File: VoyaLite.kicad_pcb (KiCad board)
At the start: 4 copper layers, 141.4 x 143 mm, 72 parts, among them J1 Conn_01x02_Socket, J3 USB_C_Receptacle_USB2.0_16P, J4 Conn_01x04_Socket, Q1 NTJD1155LT1G, Q2 NTJD1155LT1G, SW1 SW_SPDT_312, SW2 SW_SPDT_312, U1 WE-TVS-82400102, U2 E73-2G4M08S1C, U3 BQ24075RGT, U4 XC6220B331MR, Y1 32.768kHz

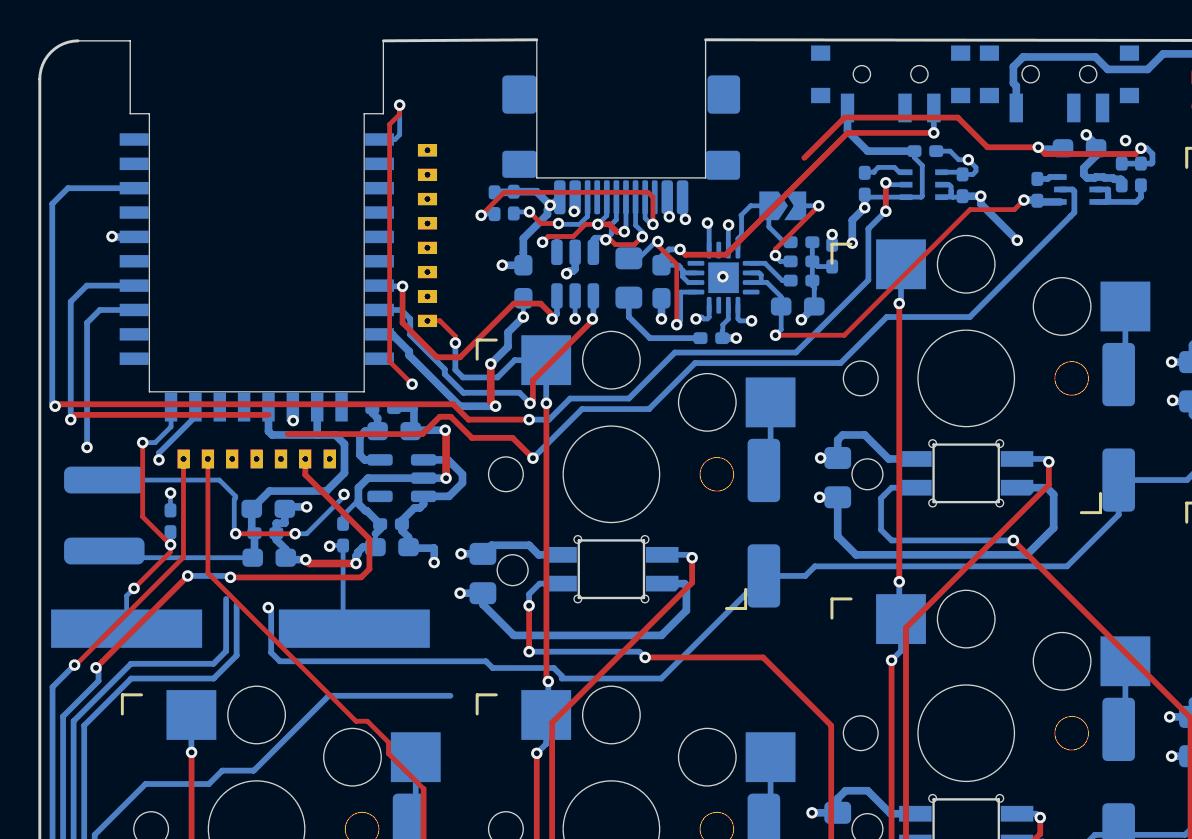
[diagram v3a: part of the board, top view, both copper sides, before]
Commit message: add voyalite
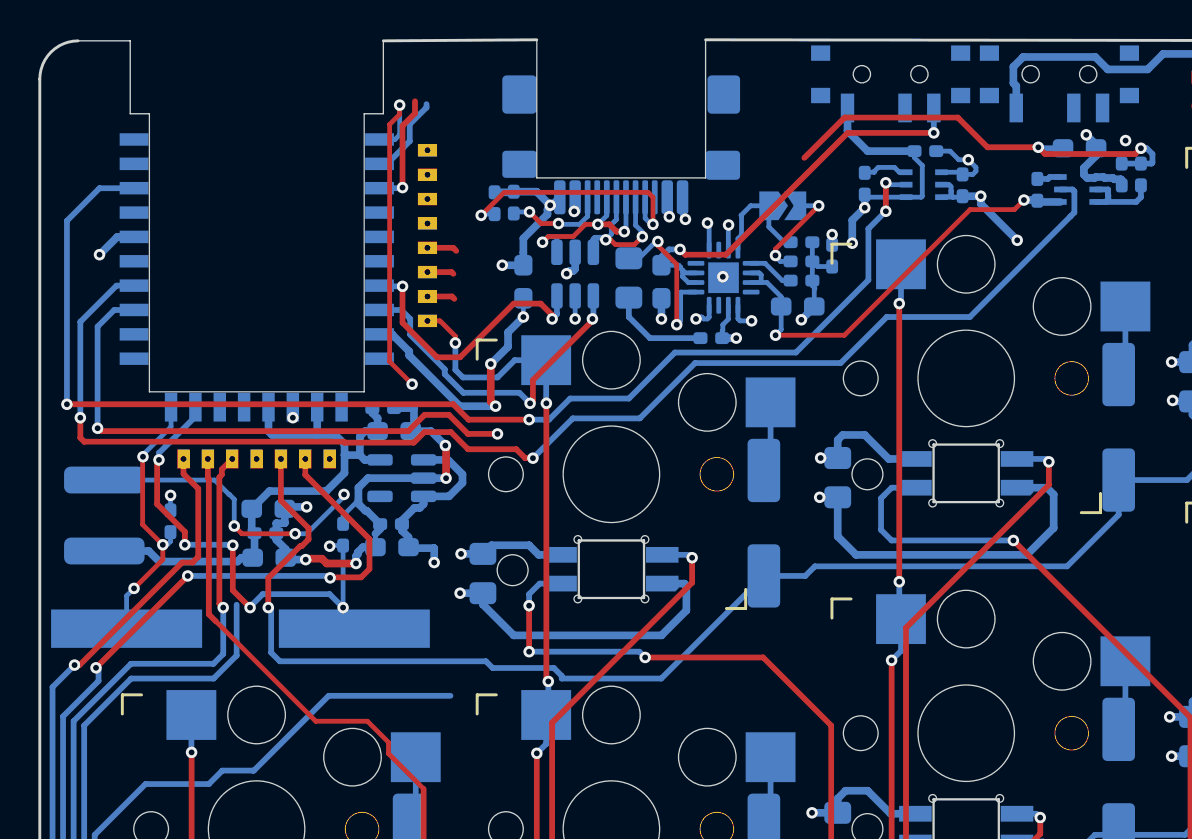
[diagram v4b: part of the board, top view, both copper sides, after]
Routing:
- net BAT_MEAS_ADC: track 32.7 -> 52.7 mm, vias 3 -> 4
- net Net-(U2B-P0.01/XL2): track 8.83 -> 25.6 mm, vias 2 -> 6
- net r5: track 127.3 -> 136.5 mm
- net r2: track 274.9 -> 282.5 mm, vias 0 -> 1
- net Net-(J4-Pin_4): track 13.3 -> 19.3 mm, vias 0 -> 1
- net r3: track 182.4 -> 186.7 mm
- net LED_EN: track 67.6 -> 65.5 mm
- net c5: track 75.3 -> 76.9 mm
- net GND: track 1316.1 -> 1317.5 mm
- net c3: track 75.2 -> 76.6 mm
- net c4: track 75.5 -> 76.9 mm
- net BAT_MEAS_EN: track 70.8 -> 69.5 mm
- net LED: track 88.9 -> 90.1 mm
- net c7: track 226.4 -> 227.6 mm
- net +3V3: track 29.1 -> 30.0 mm

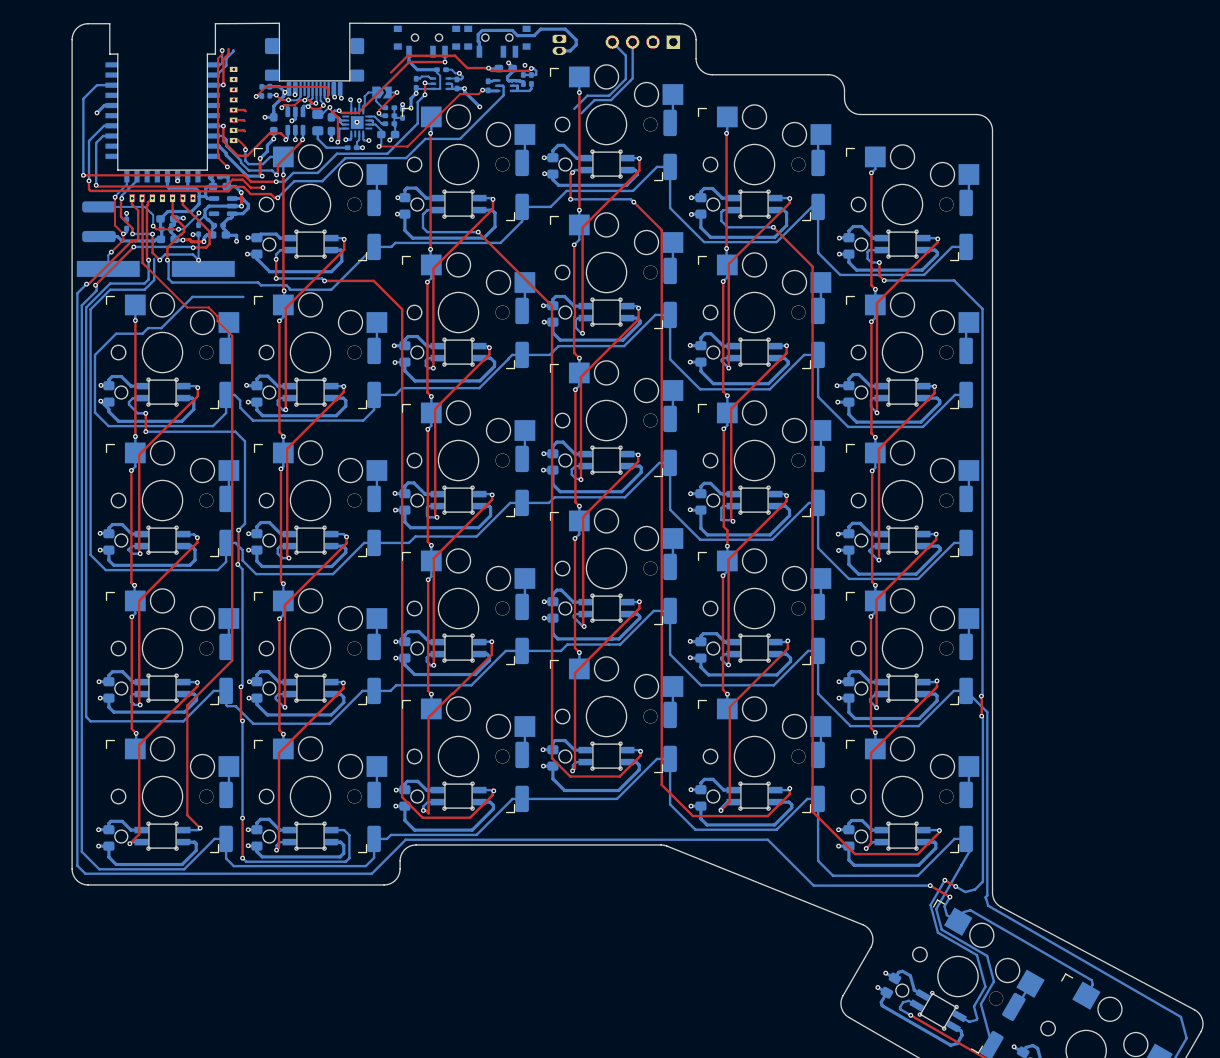
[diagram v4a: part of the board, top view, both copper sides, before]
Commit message: add changes to voyalite. Add nrf52840 plus
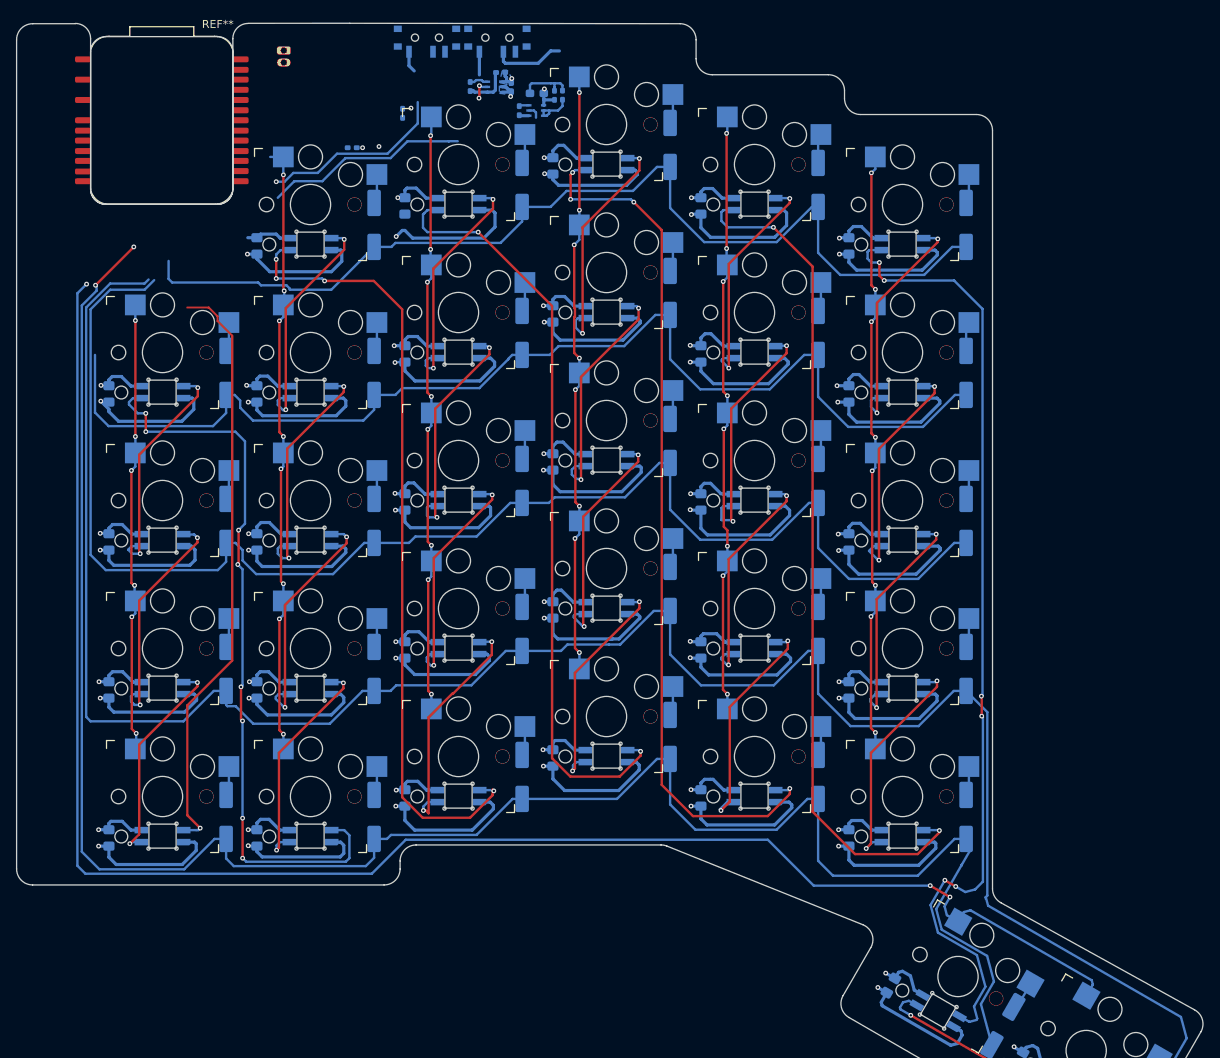
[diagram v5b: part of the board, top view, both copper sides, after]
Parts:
- removed C1, C34, C37, C38, C39: 4u7, Capacitor_SMD:C_0603_1608Metric_Pad1.08x0.95mm_HandSolder
- removed C40, C43, C44: 100n, Capacitor_SMD:C_0402_1005Metric_Pad0.74x0.62mm_HandSolder
- removed C41, C42: 10u, Capacitor_SMD:C_0603_1608Metric_Pad1.08x0.95mm_HandSolder
- removed C47, C49: 7p, Capacitor_SMD:C_0402_1005Metric_Pad0.74x0.62mm_HandSolder
- removed D1: Orange, Diode_SMD:D_0805_2012Metric_Pad1.15x1.40mm_HandSolder
- removed J3: USB_C_Receptacle_USB2.0_16P, Library_Pia:USB_C_Receptacle_Bottom_Up SMD
- removed J4: Conn_01x04_Socket, Connector_PinHeader_2.54mm:PinHeader_1x04_P2.54mm_Vertical
- removed JP1: SolderJumper_2_Open, Jumper:SolderJumper-2_P1.3mm_Open_TrianglePad1.0x1.5mm
- removed L1: 10uH, Inductor_SMD:L_APV_ANR5045
- removed R1, R2: 10K, Capacitor_SMD:C_0402_1005Metric_Pad0.74x0.62mm_HandSolder
- removed R3, R4: 51K, Capacitor_SMD:C_0402_1005Metric_Pad0.74x0.62mm_HandSolder
- removed R7: 2K, Capacitor_SMD:C_0402_1005Metric_Pad0.74x0.62mm_HandSolder
- removed U1: WE-TVS-82400102, Package_TO_SOT_SMD:SOT-23-6
- removed U2: E73-2G4M08S1C, Library_Pia:E73-2G4M08S1C-52840 - reverse
- removed U3: BQ24075RGT, Package_DFN_QFN:VQFN-16-1EP_3x3mm_P0.5mm_EP1.6x1.6mm
- removed U4: XC6220B331MR, Package_TO_SOT_SMD:SOT-23-5
- removed Y1: 32.768kHz, Crystal:Crystal_SMD_HC49-SD_HandSoldering
- added REF**: MCU_Seeed_nRF52840, Library_Pia:MCU_Seeed_nRF52840, F.Cu at (65.2, 42.3)
- moved J1 34.5 mm to (80.4, 33.6)
- moved C45 7.40 mm to (107.5, 36.3)
- moved C46 6.76 mm to (108.8, 38.2)
- moved Q1 6.76 mm to (106.8, 38.1)
- moved R6 6.76 mm to (103.7, 38.1)
- moved R8 4.97 mm to (109.8, 41.1)
- moved C48 4.97 mm to (112.0, 38.9)
- moved Q2 4.97 mm to (112.0, 41.1)
- moved R9 4.36 mm to (114.2, 39.2)
- moved R10 4.35 mm to (115.2, 39.2)
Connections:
- SW1 pad 1: unconnected-(SW1-B-Pad1) -> +BATT
- SW1 pad 2: unconnected-(SW1-C-Pad2) -> /VBATIn
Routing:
- net GND: track 1317.5 -> 1140.3 mm, vias 51 -> 33
- net VBUS: track 83.5 -> 0.00 mm, vias 8 -> 0
- net BAT_MEAS_ADC: track 52.7 -> 7.37 mm, vias 4 -> 0
- net BAT_MEAS_EN: track 69.5 -> 27.1 mm, vias 2 -> 0
- net r4: track 185.0 -> 145.5 mm, vias 2 -> 0
- net LED_EN: track 65.5 -> 26.0 mm, vias 4 -> 3
- net +3V3: track 30.0 -> 0.00 mm
- net +3V8: track 59.1 -> 30.0 mm, vias 4 -> 2
- net Net-(U2B-P0.01/XL2): track 25.6 -> 0.00 mm, vias 6 -> 0
- net +BATT: track 29.4 -> 4.13 mm, vias 3 -> 1
- net Net-(SW2-A): track 22.0 -> 0.00 mm, vias 2 -> 0
- net Net-(J4-Pin_4): track 19.3 -> 0.00 mm, vias 1 -> 0
- net Net-(U2A-DM): track 17.5 -> 0.00 mm, vias 2 -> 0
- net r1: track 268.2 -> 251.4 mm, vias 3 -> 2
- net LED: track 90.1 -> 74.1 mm
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- added copper zone on B.Cu, net GND
- added copper zone on B.Cu, net VCC
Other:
- board size 141.4 x 143 mm -> 148.3 x 143 mm

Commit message: add newer files
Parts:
- removed C36: 1u, Capacitor_SMD:C_0402_1005Metric_Pad0.74x0.62mm_HandSolder
- removed R5: 10K, Capacitor_SMD:C_0402_1005Metric_Pad0.74x0.62mm_HandSolder
- removed REF**: MCU_Seeed_nRF52840, Library_Pia:MCU_Seeed_nRF52840
- removed SW1, SW2: SW_SPDT_312, Button_Switch_SMD:SW_SPDT_PCM12
- added BT1: Battery_Cell, Pia_Lib:Batteriehalter AAA_Metall, F.Cu at (48.5, 123.6)
- added J2: Conn_01x01_Pin, RT-Library:Testpoint-pad, F.Cu at (45.1, 60.7)
- added U6: XIAO-NRF82840-Plus, Pia_Lib:MCU_Seeed_nRF52840, B.Cu at (62.0, 42.3)
- J1: value Conn_01x02_Socket -> Conn_01x01_Pin; footprint Connector_JST:JST_ZH_B2B-ZR_1x02_P1.50mm_Vertical -> RT-Library:Testpoint-pad; moved to F.Cu
- Q1, Q2: footprint Library_Pia:TRANS_NTJD1155LT1G -> Pia_Lib:TRANS_NTJD1155LT1G
- S1, S10, S11, S12, S13, S14, S15, S16, S17, S18, S19, S2, S20, S21, S22, S23, S24, S25, S26, S27, S28, S29, S3, S30, S31, S4, S5, S6, S7, S8, S9: footprint Library_Pia:Kailh_Low-Profile-Switch_17mm_one Side -> Pia_Lib:Kailh_Low-Profile-Switch_17mm_one Side
- moved J1 41.0 mm to (49.7, 60.7)
- moved C45 8.07 mm to (99.4, 36.2)
- moved C46 8.07 mm to (100.7, 38.0)
- moved Q1 8.07 mm to (98.7, 38.0)
- moved R6 8.07 mm to (95.6, 37.9)
- moved R10 7.94 mm to (107.5, 41.1), turned to 0 degrees
- moved Q2 7.15 mm to (105.6, 37.8), turned to 90 degrees
- moved R8 6.90 mm to (105.6, 35.7), turned to 0 degrees
- moved R9 6.78 mm to (107.5, 40.1), turned to 180 degrees
- moved C48 4.41 mm to (107.8, 37.9), turned to -90 degrees
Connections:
- C45 pad 1: +3V8 -> +BATT
- J1 pad 1: GND -> +BATT
- Q1 pad 4: +3V8 -> +BATT
- R6 pad 1: +3V8 -> +BATT
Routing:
- net +3V8: track 30.0 -> 0.00 mm, vias 2 -> 0
- net (no net): track 0.00 -> 24.8 mm
- net +BATT: track 4.13 -> 16.5 mm, vias 1 -> 2
- net /VBATIn: track 8.95 -> 0.00 mm
- net LED_EN: track 26.0 -> 23.3 mm
- net GND: track 1140.3 -> 1142.7 mm
- added copper zone on In1.Cu, net (none)
- removed copper zone on In1.Cu, net VBUS
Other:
- board size 148.3 x 143 mm -> 153 x 143 mm

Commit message: add final changes
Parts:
- added C1: 100n, Capacitor_SMD:C_0402_1005Metric_Pad0.74x0.62mm_HandSolder, B.Cu at (74.0, 36.3)
- added C2: 1u, Capacitor_SMD:C_0402_1005Metric_Pad0.74x0.62mm_HandSolder, F.Cu at (47.5, 66.9)
- added C3: 100n, Capacitor_SMD:C_0402_1005Metric_Pad0.74x0.62mm_HandSolder, F.Cu at (47.5, 65.8)
- J1, J2: moved to B.Cu
- U6: moved to F.Cu
- moved R8 46.9 mm to (65.2, 59.6), turned to 90 degrees
- moved R6 45.6 mm to (55.5, 59.6)
- moved C45 45.6 mm to (59.3, 57.8)
- moved Q1 45.6 mm to (58.6, 59.6)
- moved C46 45.2 mm to (61.0, 59.6)
- moved C48 44.8 mm to (67.4, 57.5), turned to 0 degrees
- moved Q2 44.0 mm to (67.3, 59.6), turned to 180 degrees
- moved R9 41.8 mm to (69.6, 57.7), turned to -90 degrees
- moved R10 40.5 mm to (70.6, 57.7), turned to 90 degrees
- moved J2 4.78 mm to (49.5, 62.4)
- moved J1 4.35 mm to (45.7, 62.4)
- turned U6 to 0 degrees
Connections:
- U6 pad 12: +BATT -> unconnected-(U6-P0.31/BAT/D16-Pad12)
- U6 pad 22: unconnected-(U6-GND-Pad22) -> GND
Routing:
- net c6: track 75.6 -> 211.2 mm, vias 8 -> 10
- net c5: track 75.3 -> 194.7 mm, vias 8 -> 10
- net c4: track 75.5 -> 176.9 mm, vias 8 -> 10
- net c3: track 75.2 -> 163.7 mm, vias 8 -> 10
- net GND: track 1142.7 -> 1230.5 mm, vias 33 -> 35
- net +BATT: track 16.5 -> 103.0 mm, vias 2 -> 1
- net LED: track 74.1 -> 134.5 mm, vias 1 -> 2
- net VCC: track 784.1 -> 844.5 mm, vias 31 -> 34
- net c2: track 76.8 -> 136.7 mm, vias 8 -> 10
- net r4: track 145.5 -> 189.1 mm
- net c1: track 56.4 -> 99.4 mm, vias 6 -> 8
- net r5: track 127.1 -> 167.2 mm
- net r1: track 251.4 -> 283.9 mm, vias 2 -> 0
- net r2: track 272.0 -> 303.5 mm
- net r3: track 179.7 -> 209.8 mm
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- added copper zone on F.Cu, net +BATT
- removed copper zone on In1.Cu, net (none)
- removed copper zone on In1.Cu, net +BATT
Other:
- board text added: "+"
- board text added: "-"
